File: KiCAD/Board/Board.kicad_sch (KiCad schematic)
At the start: 106 parts, among them J1 MOTOR_5PIN_CONNECTOR, J2 MOTOR_5PIN_CONNECTOR_2, J3 BATTERY_2PIN_CONNECTOR, Q1 SFH309, Q5 SFH309, Q7 AO3400A, U1 4040, U10 ULN2003A, U11 CD4060BE, U2 4015, U5 4040, U8 LM7805_TO220, U9 LM393, Y1 Crystal

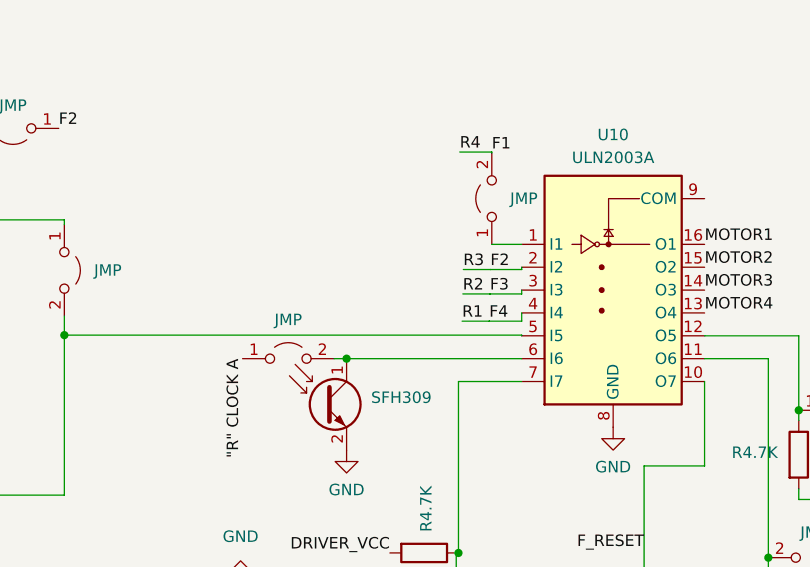
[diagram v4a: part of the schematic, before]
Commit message: June 3rd 2025 Update
Added ULN2003 Pull down Resistors for Stepper Motor Control
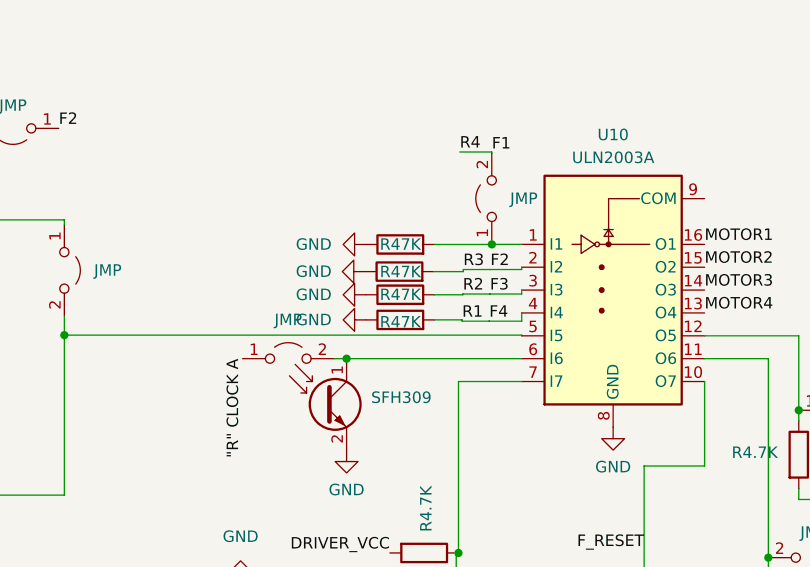
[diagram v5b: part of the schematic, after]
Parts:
- added R19, R24, R25, R26: R47K, Resistor_THT:R_Axial_DIN0207_L6.3mm_D2.5mm_P10.16mm_Horizontal, symbol Device:R
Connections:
- net F2: now also R24.2
- net F3: now also R25.2
- net F4: now also R26.2
- net GND: now also R19.1, R24.1, R25.1, R26.1
- net at JP15.1 (A), U10.1 (I1): now also R19.2
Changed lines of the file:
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@@
   (junction (at 121.0759 234.9305) (diameter 0) (color 0 0 0 0)
   )
+  (junction (at 203.2122 272.7859) (diameter 0) (color 0 0 0 0)
+  )
   (junction (at 165.608 107.7009) (diameter 0) (color 0 0 0 0)
   )
@@
     (stroke (width 0) (type default))
   )
+  (wire (pts (xy 199.9101 281.178) (xy 199.9101 281.3197))
+    (stroke (width 0) (type default))
+  )
   (wire (pts (xy 199.2567 311.43) (xy 184.3383 311.43))
     (stroke (width 0) (type default))
   )
+  (wire (pts (xy 196.85 281.178) (xy 199.9101 281.178))
+    (stroke (width 0) (type default))
+  )
   (wire (pts (xy 314.9568 103.886) (xy 314.9568 131.8607))
     (stroke (width 0) (type default))
@@
     (stroke (width 0) (type default))
   )
+  (wire (pts (xy 196.85 278.384) (xy 199.9863 278.384))
+    (stroke (width 0) (type default))
+  )
   (wire (pts (xy 126.873 53.3449) (xy 126.873 56.388))
     (stroke (width 0) (type default))
@@
     (stroke (width 0) (type default))
   )
+  (wire (pts (xy 199.9863 278.384) (xy 199.9863 278.2971))
+    (stroke (width 0) (type default))
+  )
   (wire (pts (xy 137.3065 259.8987) (xy 137.3065 270.0587))
     (stroke (width 0) (type default))
@@
     (stroke (width 0) (type default))
   )
+  (wire (pts (xy 203.2122 272.7859) (xy 206.5274 272.7859))
+    (stroke (width 0) (type default))
+  )
   (wire (pts (xy 132.588 82.6399) (xy 132.588 82.423))
     (stroke (width 0) (type default))
@@
     (stroke (width 0) (type default))
   )
+  (wire (pts (xy 196.7567 275.8115) (xy 200.0371 275.8115))
+    (stroke (width 0) (type default))
+  )
   (wire (pts (xy 165.608 92.583) (xy 178.4983 92.583))
     (stroke (width 0) (type default))
@@
     (stroke (width 0) (type default))
   )
+  (wire (pts (xy 200.0371 275.8115) (xy 200.0371 275.5793))
+    (stroke (width 0) (type default))
+  )
   (wire (pts (xy 199.2567 311.43) (xy 199.2567 307.0739))
     (stroke (width 0) (type default))
@@
     (stroke (width 0) (type default))
   )
-  (wire (pts (xy 203.204 272.7859) (xy 206.5274 272.7859))
+  (wire (pts (xy 203.204 272.7859) (xy 203.2122 272.7859))
     (stroke (width 0) (type default))
   )
@@
     (stroke (width 0) (type default))
   )
+  (wire (pts (xy 203.2122 272.796) (xy 203.2122 272.7859))
+    (stroke (width 0) (type default))
+  )
   (wire (pts (xy 171.5875 327.2799) (xy 171.5875 326.0243))
     (stroke (width 0) (type default))
@@
     (stroke (width 0) (type default))
   )
+  (wire (pts (xy 196.85 272.796) (xy 203.2122 272.796))
+    (stroke (width 0) (type default))
+  )
   (wire (pts (xy 202.9206 281.3203) (xy 206.5274 281.3203))
     (stroke (width 0) (type default))
@@
     )
   )
+  (symbol (lib_id "power:GND") (at 189.23 278.384 270) (unit 1)
+    (in_bom yes) (on_board yes) (dnp no) (fields_autoplaced)
+    (property "Reference" "#PWR032" (at 182.88 278.384 0)
+      (effects (font (size 1.27 1.27)) hide)
+    )
+    (property "Value" "GND" (at 185.42 278.384 90)
+      (effects (font (size 1.27 1.27)) (justify right))
+    )
+    (property "Footprint" "" (at 189.23 278.384 0)
+      (effects (font (size 1.27 1.27)) hide)
+    )
+    (property "Datasheet" "" (at 189.23 278.384 0)
+      (effects (font (size 1.27 1.27)) hide)
+    )
+    (pin "1")
+    (instances
+      (project "Board"
+        (path "/f7ca7e2d-986d-4d60-b0ab-4f277bdddde6"
+          (reference "#PWR032") (unit 1)
+        )
+      )
+    )
+  )
   (symbol (lib_id "Device:C") (at 85.725 74.295 0) (unit 1)
     (in_bom yes) (on_board yes) (dnp no) (fields_autoplaced)
@@
     )
   )
+  (symbol (lib_id "Device:R") (at 192.9467 275.8115 90) (unit 1)
+    (in_bom yes) (on_board yes) (dnp no)
+    (property "Reference" "R24" (at 191.6767 273.2715 0)
+      (effects (font (size 1.27 1.27)) (justify left) hide)
+    )
+    (property "Value" "R47K" (at 190.754 275.844 90)
+      (effects (font (size 1.27 1.27)) (justify right))
+    )
+    (property "Footprint" "Resistor_THT:R_Axial_DIN0207_L6.3mm_D2.5mm_P10.16mm_Horizontal" (at 192.9467 277.5895 90)
+      (effects (font (size 1.27 1.27)) hide)
+    )
+    (property "Datasheet" "~" (at 192.9467 275.8115 0)
+      (effects (font (size 1.27 1.27)) hide)
+    )
+    (pin "2")
+    (pin "1")
+    (instances
+      (project "Board"
+        (path "/f7ca7e2d-986d-4d60-b0ab-4f277bdddde6"
+          (reference "R24") (unit 1)
+        )
+      )
+    )
+  )
   (symbol (lib_id "Device:R") (at 311.15 88.646 90) (unit 1)
     (in_bom yes) (on_board yes) (dnp no) (fields_autoplaced)
@@
     )
   )
+  (symbol (lib_id "power:GND") (at 189.23 281.178 270) (unit 1)
+    (in_bom yes) (on_board yes) (dnp no) (fields_autoplaced)
+    (property "Reference" "#PWR034" (at 182.88 281.178 0)
+      (effects (font (size 1.27 1.27)) hide)
+    )
+    (property "Value" "GND" (at 185.42 281.178 90)
+      (effects (font (size 1.27 1.27)) (justify right))
+    )
+    (property "Footprint" "" (at 189.23 281.178 0)
+      (effects (font (size 1.27 1.27)) hide)
+    )
+    (property "Datasheet" "" (at 189.23 281.178 0)
+      (effects (font (size 1.27 1.27)) hide)
+    )
+    (pin "1")
+    (instances
+      (project "Board"
+        (path "/f7ca7e2d-986d-4d60-b0ab-4f277bdddde6"
+          (reference "#PWR034") (unit 1)
+        )
+      )
+    )
+  )
   (symbol (lib_id "Device:D") (at 129.1785 264.6739 180) (unit 1)
     (in_bom yes) (on_board yes) (dnp no)
@@
     )
   )
+  (symbol (lib_id "power:GND") (at 189.1367 275.8115 270) (unit 1)
+    (in_bom yes) (on_board yes) (dnp no) (fields_autoplaced)
+    (property "Reference" "#PWR030" (at 182.7867 275.8115 0)
+      (effects (font (size 1.27 1.27)) hide)
+    )
+    (property "Value" "GND" (at 185.42 275.8115 90)
+      (effects (font (size 1.27 1.27)) (justify right))
+    )
+    (property "Footprint" "" (at 189.1367 275.8115 0)
+      (effects (font (size 1.27 1.27)) hide)
+    )
+    (property "Datasheet" "" (at 189.1367 275.8115 0)
+      (effects (font (size 1.27 1.27)) hide)
+    )
+    (pin "1")
+    (instances
+      (project "Board"
+        (path "/f7ca7e2d-986d-4d60-b0ab-4f277bdddde6"
+          (reference "#PWR030") (unit 1)
+        )
+      )
+    )
+  )
   (symbol (lib_id "power:GND") (at 73.787 35.56 0) (unit 1)
     (in_bom yes) (on_board yes) (dnp no) (fields_autoplaced)
@@
     )
   )
+  (symbol (lib_id "Device:R") (at 193.04 278.384 90) (unit 1)
+    (in_bom yes) (on_board yes) (dnp no)
+    (property "Reference" "R25" (at 191.77 275.844 0)
+      (effects (font (size 1.27 1.27)) (justify left) hide)
+    )
+    (property "Value" "R47K" (at 190.754 278.384 90)
+      (effects (font (size 1.27 1.27)) (justify right))
+    )
+    (property "Footprint" "Resistor_THT:R_Axial_DIN0207_L6.3mm_D2.5mm_P10.16mm_Horizontal" (at 193.04 280.162 90)
+      (effects (font (size 1.27 1.27)) hide)
+    )
+    (property "Datasheet" "~" (at 193.04 278.384 0)
+      (effects (font (size 1.27 1.27)) hide)
+    )
+    (pin "2")
+    (pin "1")
+    (instances
+      (project "Board"
+        (path "/f7ca7e2d-986d-4d60-b0ab-4f277bdddde6"
+          (reference "R25") (unit 1)
+        )
+      )
+    )
+  )
   (symbol (lib_id "Device:D") (at 161.798 110.363 0) (unit 1)
     (in_bom yes) (on_board yes) (dnp no)
@@
     )
   )
+  (symbol (lib_id "Device:R") (at 193.04 281.178 90) (unit 1)
+    (in_bom yes) (on_board yes) (dnp no)
+    (property "Reference" "R26" (at 191.77 278.638 0)
+      (effects (font (size 1.27 1.27)) (justify left) hide)
+    )
+    (property "Value" "R47K" (at 190.754 281.432 90)
+      (effects (font (size 1.27 1.27)) (justify right))
+    )
+    (property "Footprint" "Resistor_THT:R_Axial_DIN0207_L6.3mm_D2.5mm_P10.16mm_Horizontal" (at 193.04 282.956 90)
+      (effects (font (size 1.27 1.27)) hide)
+    )
+    (property "Datasheet" "~" (at 193.04 281.178 0)
+      (effects (font (size 1.27 1.27)) hide)
+    )
+    (pin "2")
+    (pin "1")
+    (instances
+      (project "Board"
+        (path "/f7ca7e2d-986d-4d60-b0ab-4f277bdddde6"
+          (reference "R26") (unit 1)
+        )
+      )
+    )
+  )
+  (symbol (lib_id "power:GND") (at 189.23 272.796 270) (unit 1)
+    (in_bom yes) (on_board yes) (dnp no) (fields_autoplaced)
+    (property "Reference" "#PWR023" (at 182.88 272.796 0)
+      (effects (font (size 1.27 1.27)) hide)
+    )
+    (property "Value" "GND" (at 185.42 272.796 90)
+      (effects (font (size 1.27 1.27)) (justify right))
+    )
+    (property "Footprint" "" (at 189.23 272.796 0)
+      (effects (font (size 1.27 1.27)) hide)
+    )
+    (property "Datasheet" "" (at 189.23 272.796 0)
+      (effects (font (size 1.27 1.27)) hide)
+    )
+    (pin "1")
+    (instances
+      (project "Board"
+        (path "/f7ca7e2d-986d-4d60-b0ab-4f277bdddde6"
+          (reference "#PWR023") (unit 1)
+        )
+      )
+    )
+  )
   (symbol (lib_id "Device:D") (at 161.798 87.503 180) (unit 1)
     (in_bom yes) (on_board yes) (dnp no)
@@
         )
       )
+    )
+  )
+  (symbol (lib_id "Device:R") (at 193.04 272.796 90) (unit 1)
+    (in_bom yes) (on_board yes) (dnp no)
+    (property "Reference" "R19" (at 191.77 270.256 0)
+      (effects (font (size 1.27 1.27)) (justify left) hide)
+    )
+    (property "Value" "R47K" (at 190.754 272.796 90)
+      (effects (font (size 1.27 1.27)) (justify right))
+    )
+    (property "Footprint" "Resistor_THT:R_Axial_DIN0207_L6.3mm_D2.5mm_P10.16mm_Horizontal" (at 193.04 274.574 90)
+      (effects (font (size 1.27 1.27)) hide)
+    )
+    (property "Datasheet" "~" (at 193.04 272.796 0)
+      (effects (font (size 1.27 1.27)) hide)
+    )
+    (pin "2")
+    (pin "1")
+    (instances
+      (project "Board"
+        (path "/f7ca7e2d-986d-4d60-b0ab-4f277bdddde6"
+          (reference "R19") (unit 1)
+        )
+      )

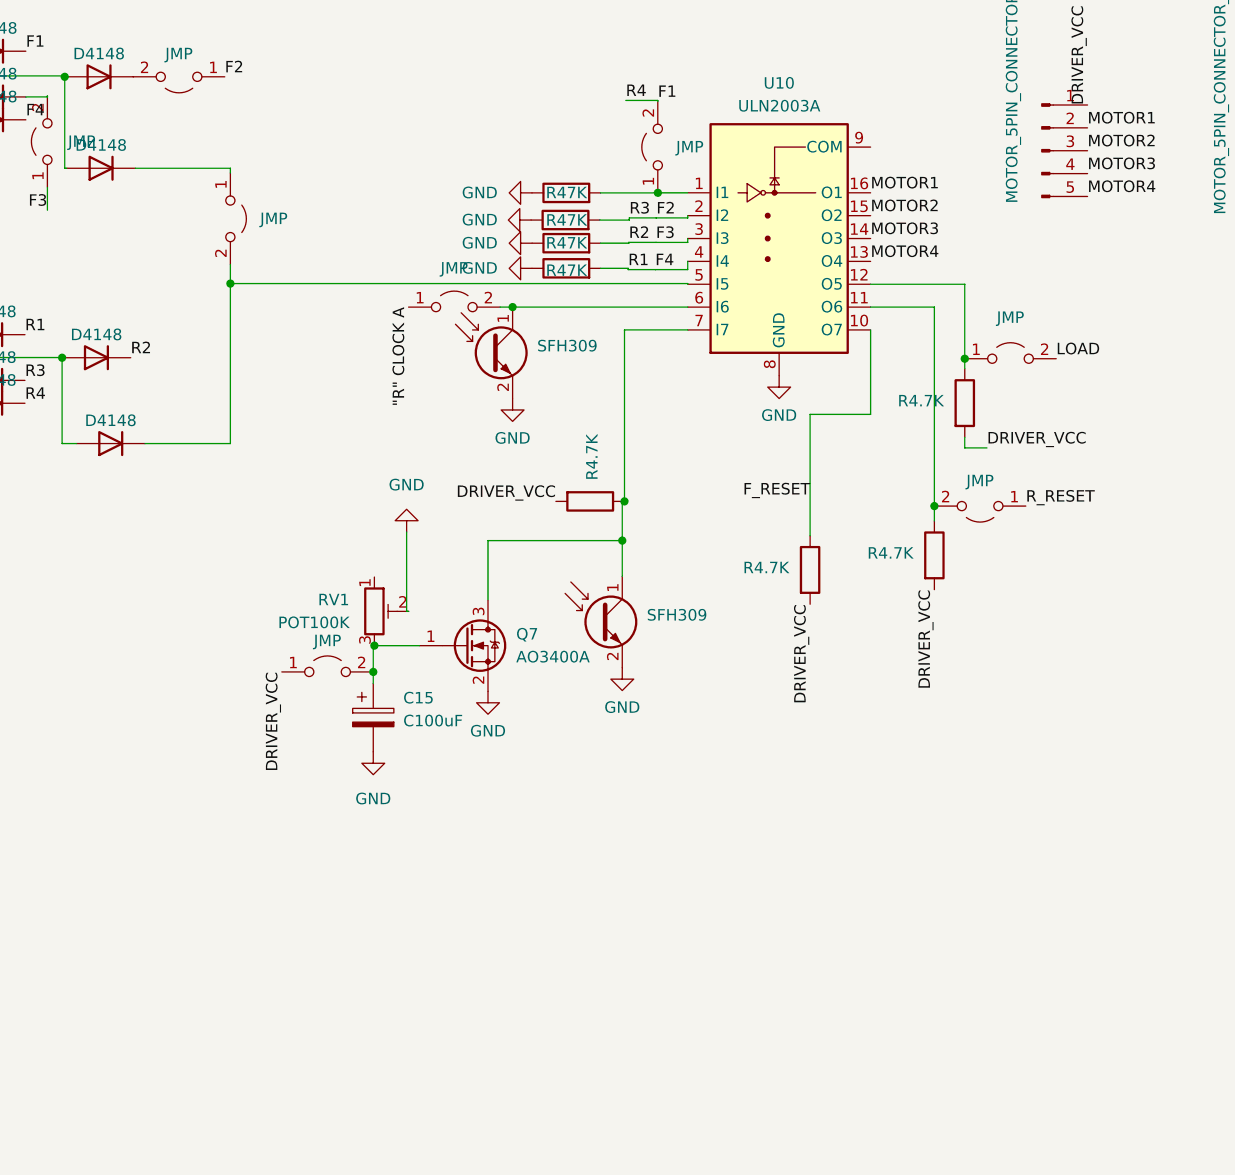
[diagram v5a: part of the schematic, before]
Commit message: 10th June 2025 Updated
Added Pull Downs 47K to ULN2003. Inverted Logic for Photo Transistors where cutting off IR rays off of photo transistors turns off forward and reverse motion since blocking IR rays is easier then reflecting it
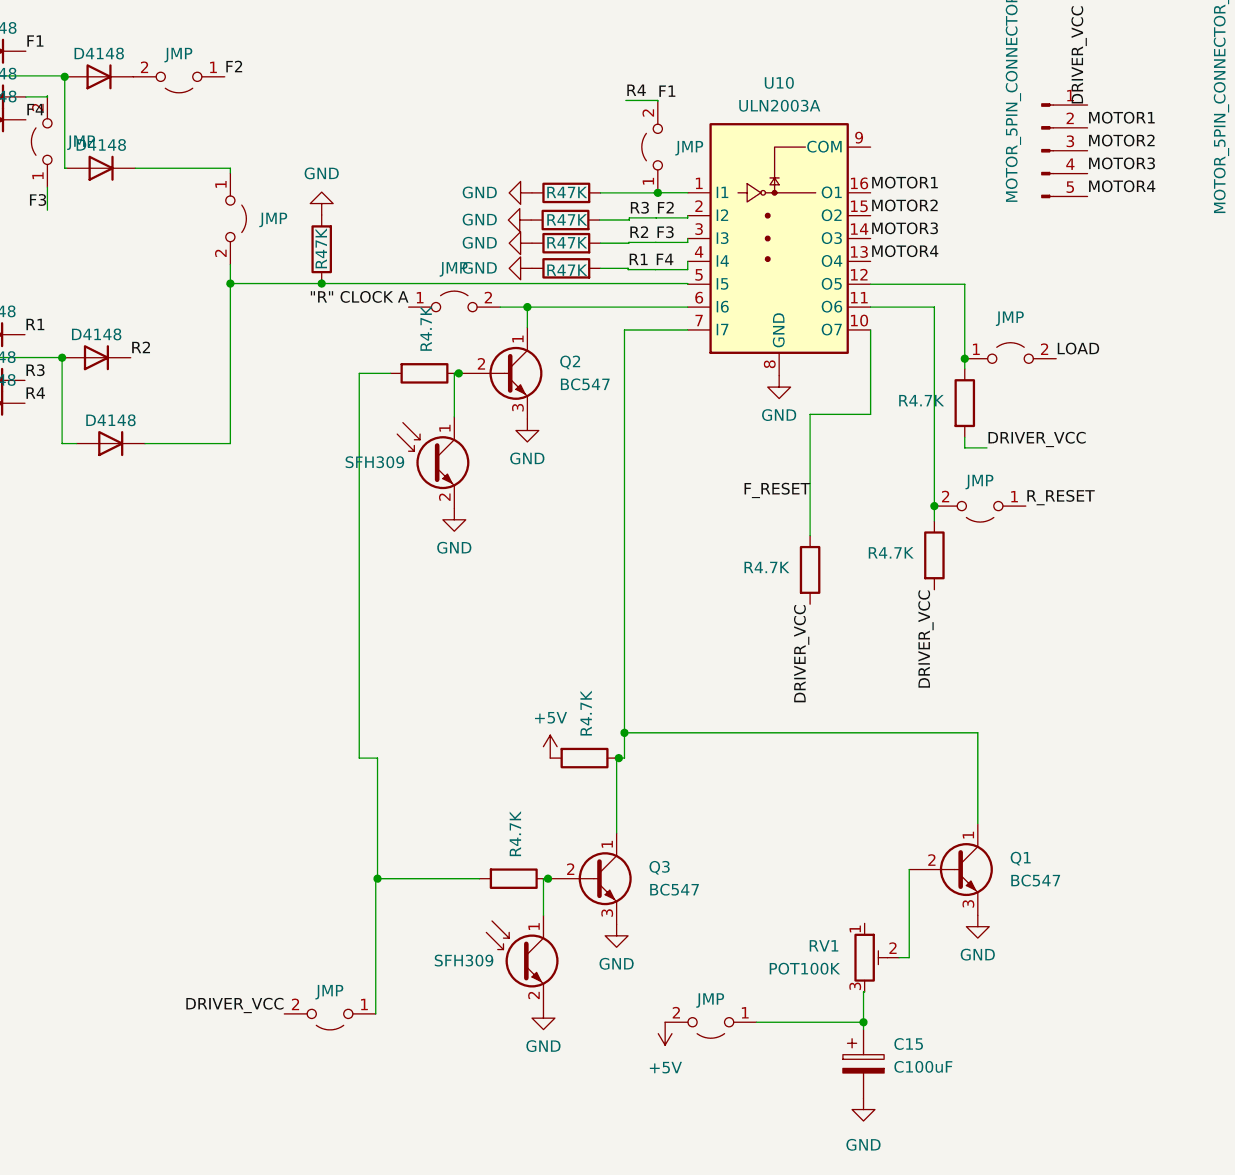
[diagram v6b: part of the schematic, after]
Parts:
- removed Q1: SFH309, LED_THT:LED_D3.0mm_Clear, symbol Sensor_Optical:SFH309
- removed Q7: AO3400A, Package_TO_SOT_SMD:SOT-23, symbol Transistor_FET:AO3400A
- added JP12: JMP, Library:Jumper, symbol Jumper:Jumper_2_Open
- added Q1, Q2, Q3: BC547, Package_TO_SOT_THT:TO-92_Inline, symbol Transistor_BJT:BC547
- added Q4: SFH309, LED_THT:LED_D3.0mm_Clear, symbol Sensor_Optical:SFH309
- added R27: R47K, Resistor_THT:R_Axial_DIN0207_L6.3mm_D2.5mm_P10.16mm_Horizontal, symbol Device:R
- added R28, R29: R4.7K, Resistor_THT:R_Axial_DIN0207_L6.3mm_D2.5mm_P10.16mm_Horizontal, symbol Device:R
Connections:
- net +5V: now also JP1.2 (B), JP12.2 (B); no longer JP1.1 (A)
- net GND: now also Q1.3 (E), Q2.3 (E), Q3.3 (E), Q4.2 (E), R27.2; no longer RV1.2
- net at JP7.2 (B), U10.6 (I6): now also Q2.1 (C); no longer Q5.1 (C)
- net at D32.1 (K), JP13.2 (B), U10.5 (I5): now also R27.1
- net at R23.1, U10.7 (I7): now also Q1.1 (C), Q3.1 (C)
- net at C15.1, RV1.3: now also JP1.1 (A); no longer JP1.2 (B)
- new net: Q1.2 (B), RV1.2
- new net: JP12.1 (A), R28.2, R29.2
- new net: Q2.2 (B), Q5.1 (C), R28.1
- new net: Q3.2 (B), Q4.1 (C), R29.1
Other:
- moved on the sheet: C15, RV1
